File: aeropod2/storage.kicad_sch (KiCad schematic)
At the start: 3 parts, among them J5 Micro_SD_Card

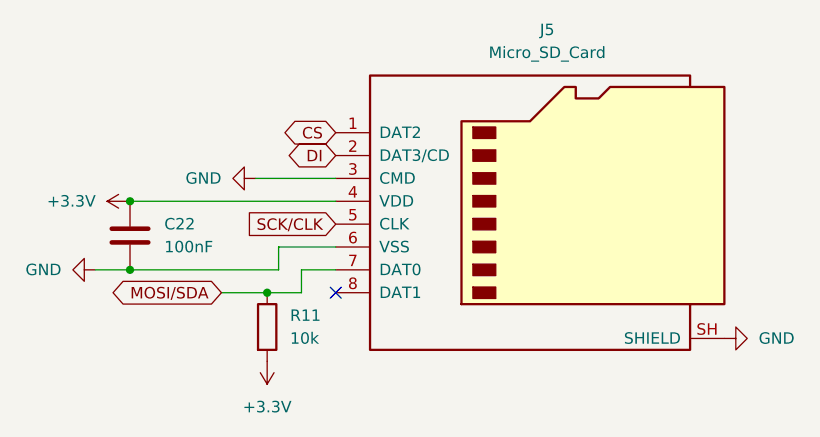
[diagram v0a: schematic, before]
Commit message: Rework the power options around battery life, not just correctness
The boost-then-LDO path on this board is the worst of the available
options for runtime: the MT3608 converts at about 88 percent and the
AMS1117 then burns the 4.8 V to 3.3 V difference as heat, so roughly 60
percent of the cell reaches the load. Repairing it is both the most
layout work and the least battery.

Documents four alternatives with rough energy numbers instead. The
default recommendation is now to delete the boost entirely and swap the
AMS1117 for an AP2114H-3.3, which is the same SOT-223 footprint and pin
order, needs no layout change, and still delivers more energy than the
repaired boost. Notes the AP2114HA variant, one letter different and
stocked alongside it, has a VIN/GND/VOUT pinout that would destroy the
board.

Also covers feeding the regulator straight from the cell for most of the
pack, a wired-in buck-boost module for the whole pack with no PCB work,
and a buck-boost IC as the proper fix for a respin.
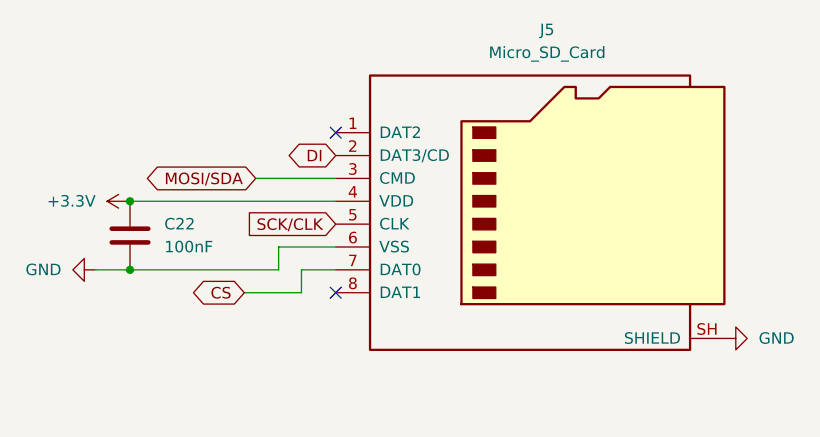
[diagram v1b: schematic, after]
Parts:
- removed R11: 10k, Resistor_SMD:R_0201_0603Metric, symbol Device:R
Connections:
- net CS: now also J5.7 (DAT0); no longer J5.1 (DAT2)
- net GND: no longer J5.3 (CMD)
- net MOSI/SDA: now also J5.3 (CMD); no longer J5.7 (DAT0)
- no-connect marks 1 -> 2

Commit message: Restore the design files to the shipped revision
The earlier revert did not fully land: KiCad had the edited sheets open
and re-saved them over the restored files, so parts of the SD rewiring
and the B5 pin move were still present in audio, esp32 and storage.

All schematics, the board file and the firmware are now restored from
d6429d0 and verified by netlist comparison rather than by diffing text.
89 nets, electrically identical to the revision the gerbers and
production files were generated from. The SD socket is back to its
original wiring and the in-progress BQ24074 power work is reverted.

Also clears two stale KiCad lock files.
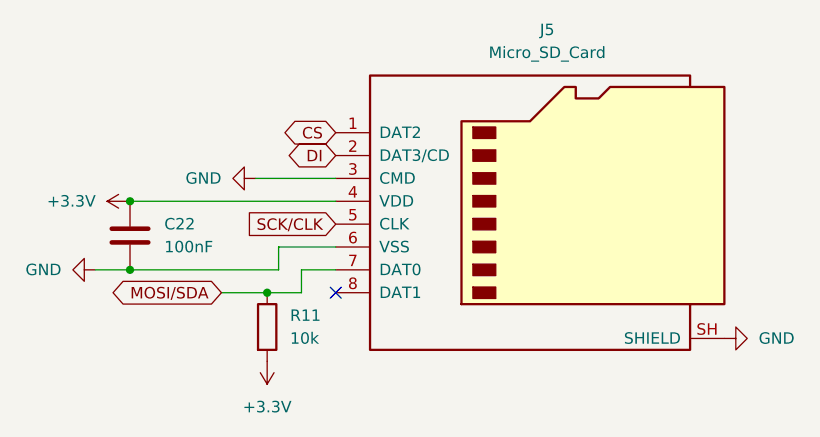
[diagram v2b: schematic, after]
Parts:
- added R11: 10k, Resistor_SMD:R_0201_0603Metric, symbol Device:R
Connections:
- net +3.3V: now also R11.2
- net CS: now also J5.1 (DAT2); no longer J5.7 (DAT0)
- net GND: now also J5.3 (CMD)
- net MOSI/SDA: now also J5.7 (DAT0), R11.1; no longer J5.3 (CMD)
- no-connect marks 2 -> 1

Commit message: Fix schematic faults found in electrical review, add reset/boot buttons
Four faults would have stopped the main board working:

- EN had no pull-up. R4/C5 sat on the unused throw of SW1 while EN was
  left holding only an AC coupled cap, so the module would not have
  booted. R4/C5 now sit on EN, and SW1/SW2 are momentary buttons to
  ground instead of slide switches.
- The microSD was miswired: connections shifted by one pin and CMD tied
  to GND, so no card could ever initialise. The display data line also
  shared a net with the card's DAT0 output. CS now lands on DAT3/CD,
  CMD on IO23 alongside the display, and IO19 is MISO from the card
  alone.
- The boost inductor was never connected to the input rail, so the
  MT3608 had nothing to pump. Rebuilt as VREGIN to L1 to SW plus diode
  anode, with the output caps and feedback divider past the diode.
- The 3.3 V rail had no headroom. R17 is now 100k, putting the boost
  near 5.1 V so the AMS1117 can actually regulate.

Also: backlight control on a new J6 pin 8 driven from IO33, 10k pull-ups
on all five button lines so GPIO35 stops floating, a 100k/100k battery
divider into IO34, both charge LEDs flipped the right way round, 33 ohm
audio series resistors instead of 470, and TP4056 set to about 400 mA.

The CP2102N auto-reset caps are gone. That package brings out RTS but no
DTR, and C30 drove IO0 from CTS, which is an input, so it could not have
worked. Flashing uses the buttons.

Firmware config.h is rewritten against the corrected schematic, and
i2s_output_init now releases the PCM5102A hardware mute on GPIO12, which
nothing was driving.

Schematic passes ERC with no new violations. The PCB has not been
re-laid-out yet, so the main board gerbers are stale; see
ELECTRICAL_REVIEW.md.
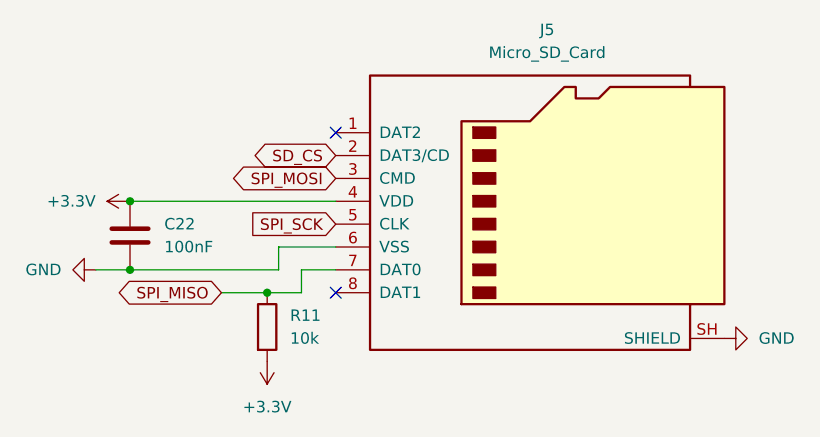
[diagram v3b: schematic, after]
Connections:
- net GND: no longer J5.3 (CMD)
- net CS: no longer names the net of J5.1 (DAT2)
- net DI renamed SD_CS
- net MOSI/SDA renamed SPI_MISO
- net SCK/CLK renamed SPI_SCK
- new net SPI_MOSI: J5.3 (CMD)
- no-connect marks 1 -> 2
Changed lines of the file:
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@@
-	(wire
-		(pts
-			(xy 105.41 99.06) (xy 114.3 99.06)
-		)
-		(stroke
-			(width 0)
-			(type default)
-		)
-	)
 	(wire
 		(pts
@@
 		)
 	)
-	(global_label "CS"
+	(global_label "SPI_MOSI"
 		(shape bidirectional)
-		(at 114.3 93.98 180)
+		(at 114.3 99.06 180)
 		(effects
 			(font
@@
 		)
 		(property "Intersheetrefs" "${INTERSHEET_REFS}"
-			(at 114.3 93.98 0)
-			(hide yes)
-			(show_name no)
-			(do_not_autoplace no)
-			(effects
-				(font
-					(size 1.27 1.27)
-				)
-			)
-		)
-	)
-	(global_label "SCK/CLK"
+			(at 114.3 99.06 0)
+			(hide yes)
+			(show_name no)
+			(do_not_autoplace no)
+			(effects
+				(font
+					(size 1.27 1.27)
+				)
+			)
+		)
+	)
+	(global_label "SPI_SCK"
 		(shape input)
 		(at 114.3 104.14 180)
@@
 		)
 	)
-	(global_label "DI"
+	(global_label "SD_CS"
 		(shape bidirectional)
 		(at 114.3 96.52 180)
@@
 		)
 	)
-	(global_label "MOSI/SDA"
+	(global_label "SPI_MISO"
 		(shape bidirectional)
 		(at 101.6 111.76 180)
@@
 	)
 	(symbol
-		(lib_id "power:GND")
-		(at 105.41 99.06 270)
-		(unit 1)
-		(body_style 1)
-		(exclude_from_sim no)
-		(in_bom yes)
-		(on_board yes)
-		(in_pos_files yes)
-		(dnp no)
-		(fields_autoplaced yes)
-		(property "Reference" "#PWR049"
-			(at 99.06 99.06 0)
-			(hide yes)
-			(show_name no)
-			(do_not_autoplace no)
-			(effects
-				(font
-					(size 1.27 1.27)
-				)
-			)
-		)
-		(property "Value" "GND"
-			(at 101.6 99.0599 90)
-			(show_name no)
-			(do_not_autoplace no)
-			(effects
-				(font
-					(size 1.27 1.27)
-				)
-				(justify right)
-			)
-		)
-		(property "Footprint" ""
-			(at 105.41 99.06 0)
-			(hide yes)
-			(show_name no)
-			(do_not_autoplace no)
-			(effects
-				(font
-					(size 1.27 1.27)
-				)
-			)
-		)
-		(property "Datasheet" ""
-			(at 105.41 99.06 0)
-			(hide yes)
-			(show_name no)
-			(do_not_autoplace no)
-			(effects
-				(font
-					(size 1.27 1.27)
-				)
-			)
-		)
-		(property "Description" "Power symbol creates a global label with name \"GND\" , ground"
-			(at 105.41 99.06 0)
-			(hide yes)
-			(show_name no)
-			(do_not_autoplace no)
-			(effects
-				(font
-					(size 1.27 1.27)
-				)
-			)
-		)
-		(pin "1"
-		)
-		(instances
-			(project "aeropod2"
-				(path "/24b34e19-463e-4d66-8262-936edb1e279f/ae5c28f8-1c97-4efc-bfa9-c7a2dc151128"
-					(reference "#PWR049")
-					(unit 1)
-				)
-			)
-		)
-	)
-	(symbol
 		(lib_id "Connector:Micro_SD_Card")
 		(at 137.16 101.6 0)
@@
 		)
 	)
+	(no_connect
+		(at 114.3 93.98)
+	)
 )

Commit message: Revert schematic, PCB and firmware to the hand-drawn version
Restores aeropod2/*.kicad_sch, aeropod2.kicad_pcb, the firmware pin map
and the BOM to their state at d6429d0, which is byte identical to the
last human-edited revision (2867710). The corrected schematic is still
in history at b35a9fa if any of it is wanted later.

The board file had picked up R18/R19 and the tactile switch footprints
from a schematic update. Nothing hand-made was lost reverting it: track
and via counts were unchanged at 894/147 and the two new parts were
sitting at KiCad's default drop position.

ELECTRICAL_REVIEW.md is rewritten to describe the faults as they stand
in this schematic, and to give the smallest set of layout changes that
makes the board work rather than the full correction.
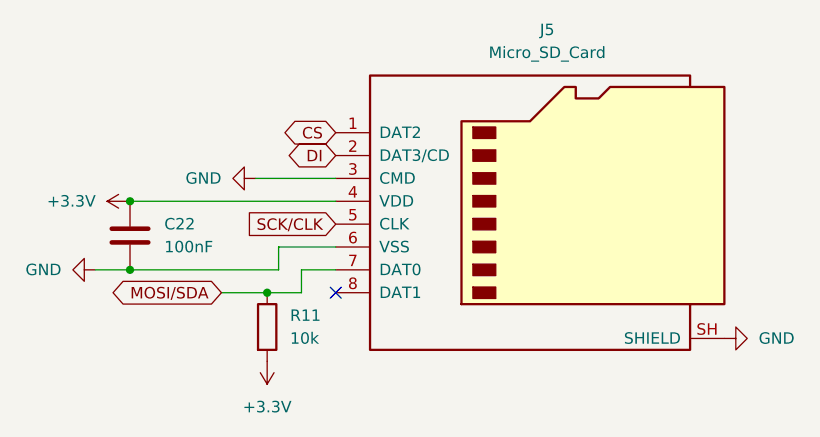
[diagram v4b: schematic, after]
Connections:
- net SPI_MOSI is gone; now on net GND: J5.3 (CMD)
- net CS: now reaches J5.1 (DAT2)
- net SD_CS renamed DI
- net SPI_MISO renamed MOSI/SDA
- net SPI_SCK renamed SCK/CLK
- no-connect marks 2 -> 1
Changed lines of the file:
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@@
+	(wire
+		(pts
+			(xy 105.41 99.06) (xy 114.3 99.06)
+		)
+		(stroke
+			(width 0)
+			(type default)
+		)
+	)
 	(wire
 		(pts
@@
 		)
 	)
-	(global_label "SPI_MOSI"
+	(global_label "CS"
 		(shape bidirectional)
-		(at 114.3 99.06 180)
+		(at 114.3 93.98 180)
 		(effects
 			(font
@@
 		)
 		(property "Intersheetrefs" "${INTERSHEET_REFS}"
-			(at 114.3 99.06 0)
-			(hide yes)
-			(show_name no)
-			(do_not_autoplace no)
-			(effects
-				(font
-					(size 1.27 1.27)
-				)
-			)
-		)
-	)
-	(global_label "SPI_SCK"
+			(at 114.3 93.98 0)
+			(hide yes)
+			(show_name no)
+			(do_not_autoplace no)
+			(effects
+				(font
+					(size 1.27 1.27)
+				)
+			)
+		)
+	)
+	(global_label "SCK/CLK"
 		(shape input)
 		(at 114.3 104.14 180)
@@
 		)
 	)
-	(global_label "SD_CS"
+	(global_label "DI"
 		(shape bidirectional)
 		(at 114.3 96.52 180)
@@
 		)
 	)
-	(global_label "SPI_MISO"
+	(global_label "MOSI/SDA"
 		(shape bidirectional)
 		(at 101.6 111.76 180)
@@
 	)
 	(symbol
+		(lib_id "power:GND")
+		(at 105.41 99.06 270)
+		(unit 1)
+		(body_style 1)
+		(exclude_from_sim no)
+		(in_bom yes)
+		(on_board yes)
+		(in_pos_files yes)
+		(dnp no)
+		(fields_autoplaced yes)
+		(property "Reference" "#PWR049"
+			(at 99.06 99.06 0)
+			(hide yes)
+			(show_name no)
+			(do_not_autoplace no)
+			(effects
+				(font
+					(size 1.27 1.27)
+				)
+			)
+		)
+		(property "Value" "GND"
+			(at 101.6 99.0599 90)
+			(show_name no)
+			(do_not_autoplace no)
+			(effects
+				(font
+					(size 1.27 1.27)
+				)
+				(justify right)
+			)
+		)
+		(property "Footprint" ""
+			(at 105.41 99.06 0)
+			(hide yes)
+			(show_name no)
+			(do_not_autoplace no)
+			(effects
+				(font
+					(size 1.27 1.27)
+				)
+			)
+		)
+		(property "Datasheet" ""
+			(at 105.41 99.06 0)
+			(hide yes)
+			(show_name no)
+			(do_not_autoplace no)
+			(effects
+				(font
+					(size 1.27 1.27)
+				)
+			)
+		)
+		(property "Description" "Power symbol creates a global label with name \"GND\" , ground"
+			(at 105.41 99.06 0)
+			(hide yes)
+			(show_name no)
+			(do_not_autoplace no)
+			(effects
+				(font
+					(size 1.27 1.27)
+				)
+			)
+		)
+		(pin "1"
+		)
+		(instances
+			(project "aeropod2"
+				(path "/24b34e19-463e-4d66-8262-936edb1e279f/ae5c28f8-1c97-4efc-bfa9-c7a2dc151128"
+					(reference "#PWR049")
+					(unit 1)
+				)
+			)
+		)
+	)
+	(symbol
 		(lib_id "Connector:Micro_SD_Card")
 		(at 137.16 101.6 0)
@@
 		)
 	)
-	(no_connect
-		(at 114.3 93.98)
-	)
 )
